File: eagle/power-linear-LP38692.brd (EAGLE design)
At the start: 32 x 24 mm, 14 parts, among them U1 LP38692

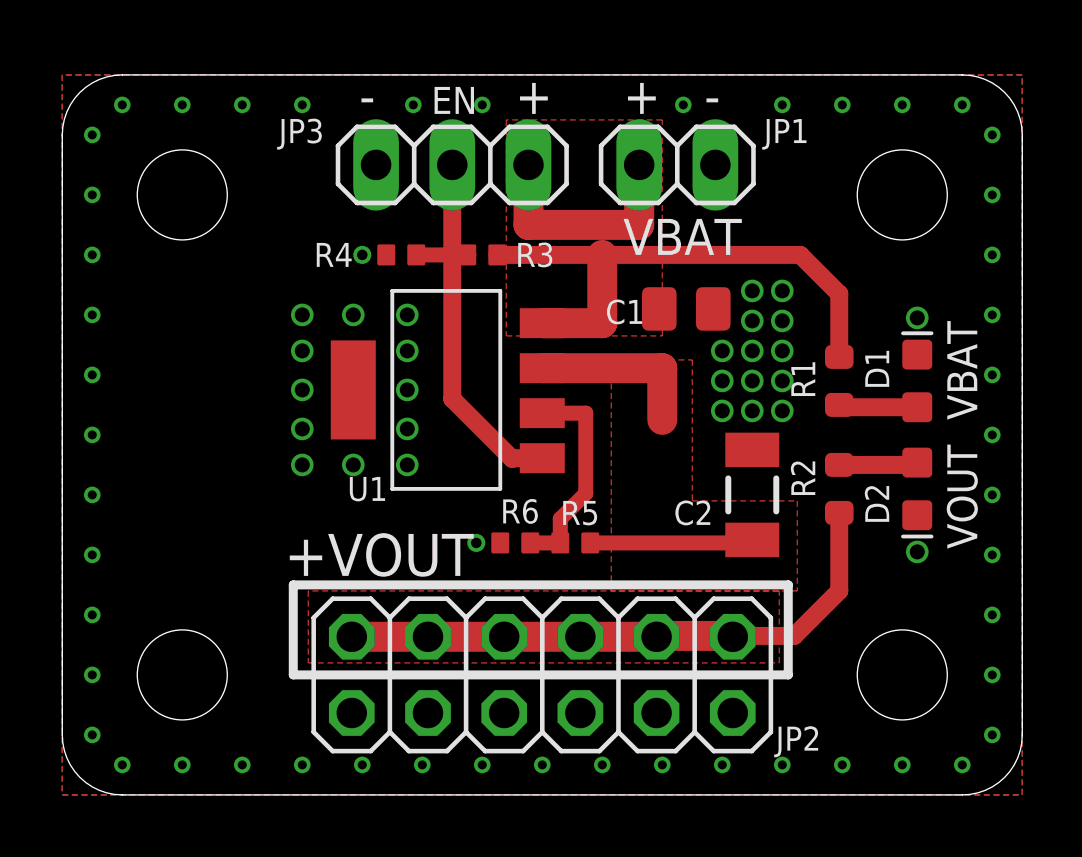
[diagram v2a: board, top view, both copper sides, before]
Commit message: Power boards add gnd for mounts
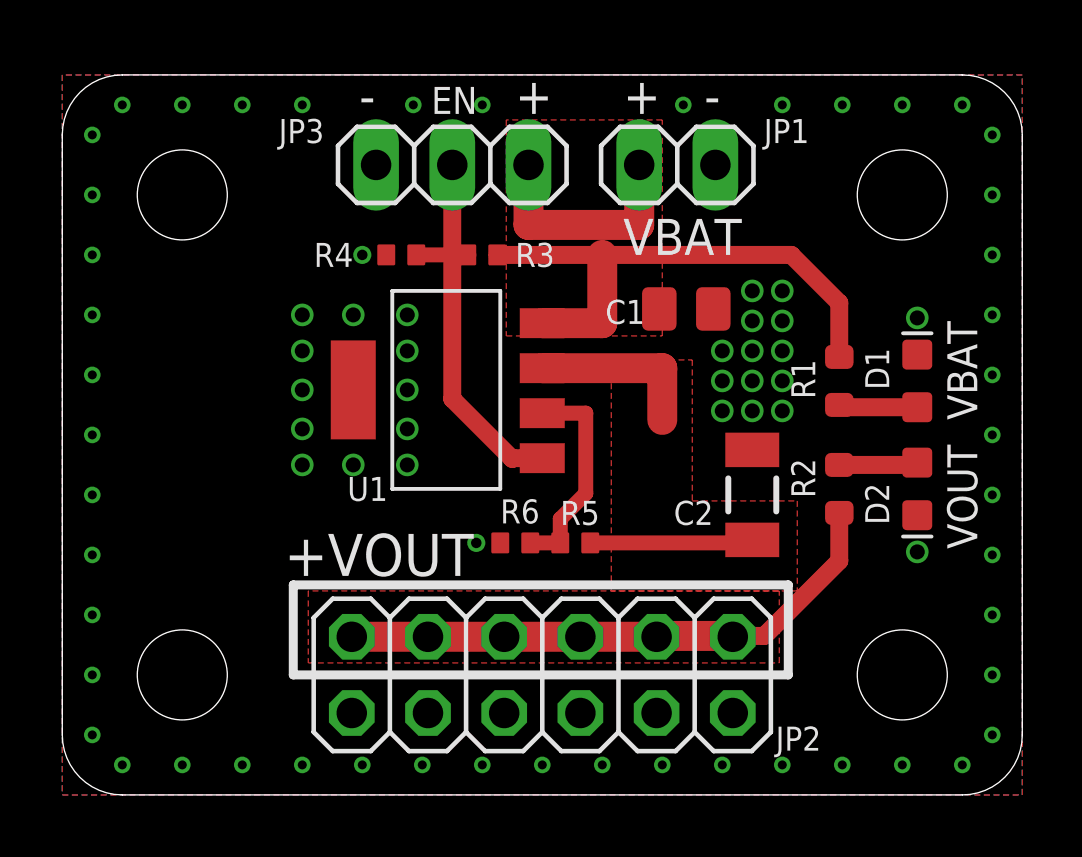
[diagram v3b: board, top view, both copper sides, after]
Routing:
- net +VOUT: track 30.7 -> 30.1 mm
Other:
- board text added: "LDO Reg LP38692 fix/adj PSAS / OreSat 2019-09-12 v1.0 E.M. - KJ7AOG"
- board text removed: "LDO Reg LP38692 fix/adj PSAS / OreSat 2019-09-08 v1.0 E.M. - KJ7AOG"
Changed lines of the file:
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@@
 <layer number="20" name="Dimension" color="24" fill="1" visible="yes" active="yes"/>
 <layer number="21" name="tPlace" color="7" fill="1" visible="yes" active="yes"/>
-<layer number="22" name="bPlace" color="7" fill="1" visible="no" active="yes"/>
+<layer number="22" name="bPlace" color="7" fill="1" visible="yes" active="yes"/>
 <layer number="23" name="tOrigins" color="15" fill="1" visible="yes" active="yes"/>
 <layer number="24" name="bOrigins" color="15" fill="1" visible="yes" active="yes"/>
@@
 <layer number="27" name="tValues" color="7" fill="1" visible="yes" active="yes"/>
 <layer number="28" name="bValues" color="7" fill="1" visible="yes" active="yes"/>
-<layer number="29" name="tStop" color="7" fill="3" visible="no" active="yes"/>
-<layer number="30" name="bStop" color="7" fill="6" visible="no" active="yes"/>
+<layer number="29" name="tStop" color="7" fill="3" visible="yes" active="yes"/>
+<layer number="30" name="bStop" color="7" fill="6" visible="yes" active="yes"/>
 <layer number="31" name="tCream" color="7" fill="4" visible="no" active="yes"/>
 <layer number="32" name="bCream" color="7" fill="5" visible="no" active="yes"/>
@@
 <text x="9.9" y="22.7" size="1.2" layer="21" font="vector" ratio="15">-</text>
 <text x="21.4" y="22.7" size="1.2" layer="21" font="vector" ratio="15">-</text>
-<text x="7.2" y="13.9" size="1.2" layer="22" font="vector" ratio="15" rot="SMR180">LDO Reg LP38692 fix/adj
+<text x="6" y="14.2" size="1.2" layer="22" font="vector" ratio="15" rot="SMR180">LDO Reg LP38692 fix/adj
 PSAS / OreSat
-2019-09-08  v1.0
+2019-09-12  v1.0
 E.M. - KJ7AOG</text>
+<circle x="4" y="20" radius="2" width="3" layer="29"/>
+<circle x="4" y="4" radius="2" width="3" layer="29"/>
+<circle x="28" y="4" radius="2" width="3" layer="29"/>
+<circle x="28" y="20" radius="2" width="3" layer="29"/>
+<circle x="28" y="20" radius="2" width="3" layer="30"/>
+<circle x="28" y="4" radius="2" width="3" layer="30"/>
+<circle x="4" y="4" radius="2" width="3" layer="30"/>
+<circle x="4" y="20" radius="2" width="3" layer="30"/>
 </plain>
 <attributes>
@@
 <vertex x="20" y="22.5"/>
 </polygon>
-<wire x1="25.9" y1="14.6" x2="25.9" y2="16.7" width="0.6" layer="1"/>
-<wire x1="25.9" y1="16.7" x2="24.6" y2="18" width="0.6" layer="1"/>
-<wire x1="24.6" y1="18" x2="18" y2="18" width="0.6" layer="1"/>
+<wire x1="25.9" y1="14.6" x2="25.9" y2="16.4" width="0.6" layer="1"/>
+<wire x1="25.9" y1="16.4" x2="24.3" y2="18" width="0.6" layer="1"/>
+<wire x1="24.3" y1="18" x2="18" y2="18" width="0.6" layer="1"/>
 <wire x1="18" y1="18" x2="14.5" y2="18" width="0.6" layer="1"/>
 <wire x1="15.54" y1="21" x2="15.54" y2="19" width="1" layer="1"/>
@@
 <wire x1="16" y1="14.225" x2="20" y2="14.225" width="1" layer="1"/>
 <wire x1="20" y1="14.225" x2="20" y2="12.5" width="1" layer="1"/>
-<wire x1="25.9" y1="9.4" x2="25.9" y2="6.8" width="0.6" layer="1"/>
-<wire x1="25.9" y1="6.8" x2="24.4" y2="5.3" width="0.6" layer="1"/>
-<wire x1="24.4" y1="5.3" x2="22.38" y2="5.3" width="0.6" layer="1"/>
+<wire x1="25.9" y1="9.4" x2="25.9" y2="7.8" width="0.6" layer="1"/>
+<wire x1="25.9" y1="7.8" x2="23.4" y2="5.3" width="0.6" layer="1"/>
+<wire x1="23.4" y1="5.3" x2="22.38" y2="5.3" width="0.6" layer="1"/>
 <wire x1="22.38" y1="5.3" x2="22.35" y2="5.27" width="0.6" layer="1"/>
 <wire x1="9.65" y1="5.27" x2="12.19" y2="5.27" width="1" layer="1"/>
